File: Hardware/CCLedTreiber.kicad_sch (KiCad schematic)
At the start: 7 parts, among them U4 SY7200AABC

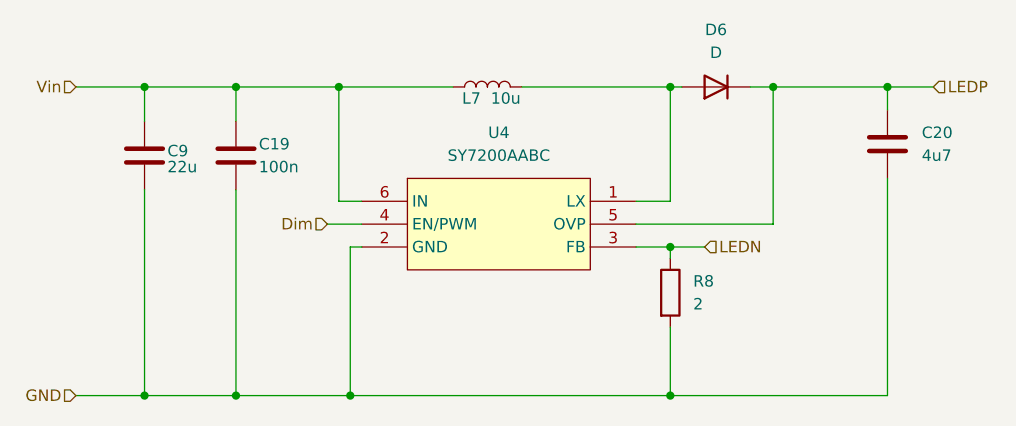
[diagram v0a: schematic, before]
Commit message: assign most LCSC numbers
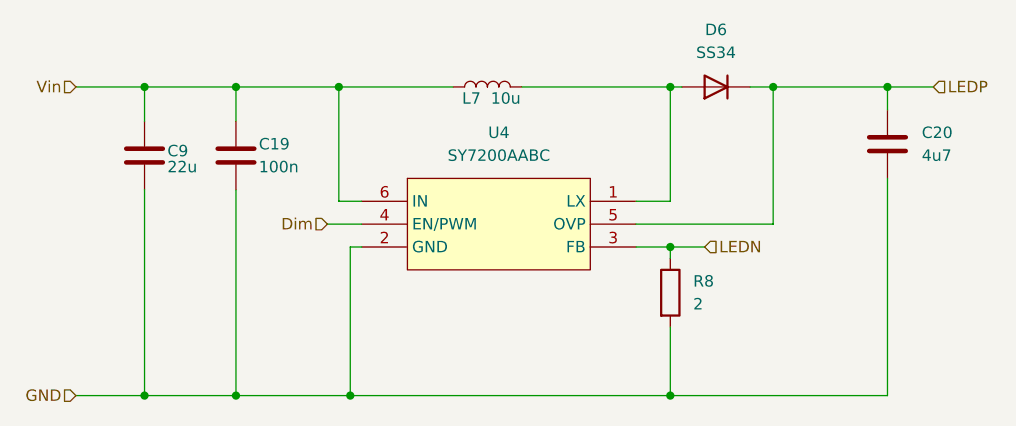
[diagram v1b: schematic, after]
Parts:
- C20: footprint Capacitor_SMD:C_1210_3225Metric -> Capacitor_SMD:C_1206_3216Metric
- D6: value D -> SS34
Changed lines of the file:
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@@
 			)
 		)
-		(property "Footprint" "Capacitor_SMD:C_1210_3225Metric"
+		(property "Footprint" "Capacitor_SMD:C_1206_3216Metric"
 			(at 150.8252 66.04 0)
 			(effects
@@
 			)
 		)
-		(property "Value" "D"
+		(property "Value" "SS34"
 			(at 130.81 52.07 0)
 			(effects

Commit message: assign remaining LCSC numbers and change R_sense of LED drivers
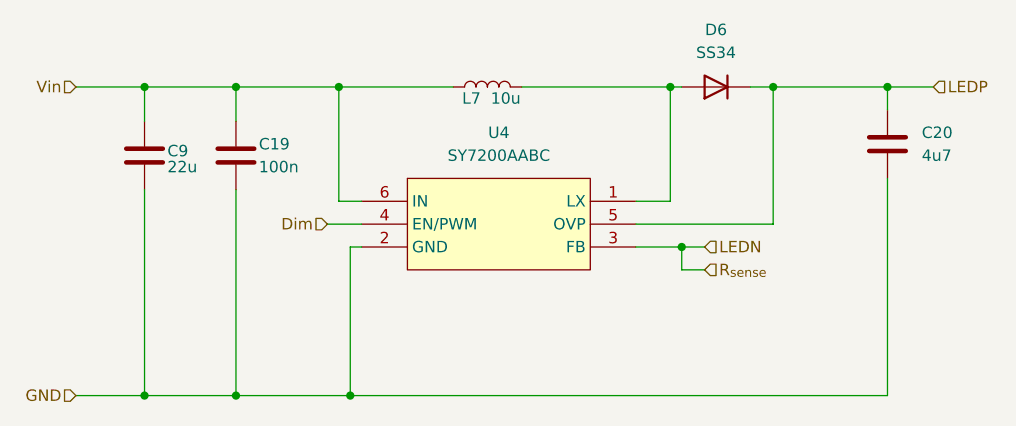
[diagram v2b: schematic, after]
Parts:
- removed R8: 2, Resistor_SMD:R_0805_2012Metric, symbol Device:R
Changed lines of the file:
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@@
 	)
 	(junction
-		(at 125.73 90.17)
-		(diameter 0)
-		(color 0 0 0 0)
-	)
-	(junction
-		(at 125.73 73.66)
+		(at 127 73.66)
 		(diameter 0)
 		(color 0 0 0 0)
@@
 	(wire
 		(pts
-			(xy 90.17 90.17) (xy 125.73 90.17)
-		)
-		(stroke
-			(width 0)
-			(type default)
-		)
-	)
-	(wire
-		(pts
-			(xy 125.73 90.17) (xy 149.86 90.17)
+			(xy 90.17 90.17) (xy 149.86 90.17)
+		)
+		(stroke
+			(width 0)
+			(type default)
+		)
+	)
+	(wire
+		(pts
+			(xy 127 73.66) (xy 129.54 73.66)
+		)
+		(stroke
+			(width 0)
+			(type default)
+		)
+	)
+	(wire
+		(pts
+			(xy 127 76.2) (xy 127 73.66)
 		)
 		(stroke
@@
 	(wire
 		(pts
-			(xy 125.73 73.66) (xy 125.73 74.93)
-		)
-		(stroke
-			(width 0)
-			(type default)
-		)
-	)
-	(wire
-		(pts
 			(xy 59.69 55.88) (xy 67.31 55.88)
 		)
@@
 	(wire
 		(pts
-			(xy 125.73 73.66) (xy 121.92 73.66)
-		)
-		(stroke
-			(width 0)
-			(type default)
-		)
-	)
-	(wire
-		(pts
 			(xy 91.44 68.58) (xy 88.9 68.58)
 		)
@@
 	(wire
 		(pts
-			(xy 125.73 82.55) (xy 125.73 90.17)
+			(xy 129.54 76.2) (xy 127 76.2)
 		)
 		(stroke
@@
 	(wire
 		(pts
-			(xy 129.54 73.66) (xy 125.73 73.66)
+			(xy 121.92 73.66) (xy 127 73.66)
 		)
 		(stroke
@@
 			(width 0)
 			(type default)
+		)
+	)
+	(hierarchical_label "R_{sense}"
+		(shape input)
+		(at 129.54 76.2 0)
+		(fields_autoplaced yes)
+		(effects
+			(font
+				(size 1.27 1.27)
+			)
+			(justify left)
 		)
 	)
@@
 					(unit 1)
 				)
-			)
-		)
-	)
-	(symbol
-		(lib_id "Device:R")
-		(at 125.73 78.74 0)
-		(unit 1)
-		(exclude_from_sim no)
-		(in_bom yes)
-		(on_board yes)
-		(dnp no)
-		(fields_autoplaced yes)
-		(property "Reference" "R8"
-			(at 128.27 77.4699 0)
-			(effects
-				(font
-					(size 1.27 1.27)
-				)
-				(justify left)
-			)
-		)
-		(property "Value" "2"
-			(at 128.27 80.0099 0)
-			(effects
-				(font
-					(size 1.27 1.27)
-				)
-				(justify left)
-			)
-		)
-		(property "Footprint" "Resistor_SMD:R_0805_2012Metric"
-			(at 123.952 78.74 90)
-			(effects
-				(font
-					(size 1.27 1.27)
-				)
-				(hide yes)
-			)
-		)
-		(property "Datasheet" "~"
-			(at 125.73 78.74 0)
-			(effects
-				(font
-					(size 1.27 1.27)
-				)
-				(hide yes)
-			)
-		)
-		(property "Description" "Resistor"
-			(at 125.73 78.74 0)
-			(effects
-				(font
-					(size 1.27 1.27)
-				)
-				(hide yes)
-			)
-		)
-		(pin "2"
-		)
-		(pin "1"
-		)
-		(instances
-			(project "LEDTischLampe"
-				(path "/34c772aa-2c68-48ca-93c3-7ad335c6d96d/510bc110-0bc9-4ffc-b901-498b8c9eef65/3158ee75-269d-4678-a09e-d51dcc288918"
-					(reference "R8")
-					(unit 1)
-				)
-				(path "/34c772aa-2c68-48ca-93c3-7ad335c6d96d/510bc110-0bc9-4ffc-b901-498b8c9eef65/9a951bb8-f46c-4ee0-a3d3-d4e6ca3ed117"
-					(reference "R26")
-					(unit 1)
-				)
-				(path "/34c772aa-2c68-48ca-93c3-7ad335c6d96d/510bc110-0bc9-4ffc-b901-498b8c9eef65/caa9cf2f-0db8-4b11-940e-edce255a092c"
-					(reference "R16")
-					(unit 1)
-				)
-				(path "/34c772aa-2c68-48ca-93c3-7ad335c6d96d/510bc110-0bc9-4ffc-b901-498b8c9eef65/fb3a6902-adb0-42f5-a319-4ea74339d4c7"
-					(reference "R27")
-					(unit 1)
-				)
-				(path "/34c772aa-2c68-48ca-93c3-7ad335c6d96d/5ca28fd6-5d3d-44e4-a7e8-e548f0114941/2a7edb5c-7ef0-4d35-9613-2c0a7f441272"
-					(reference "R9")
-					(unit 1)
-				)

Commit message: remove LCSC numbers from silkscreen (bug in jlcpcb-tools)
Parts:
- C19: LCSC (none) -> C307331
- C20: LCSC (none) -> C29823
- C9: LCSC (none) -> C52306
- D6: LCSC (none) -> C8678
- L7: LCSC (none) -> C5832376
- U4: LCSC (none) -> C107309
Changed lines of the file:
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@@
+			)
+		)
+		(property "LCSC" "C52306"
+			(at 69.85 62.992 0)
+			(effects
+				(font
+					(size 1.27 1.27)
+				)
+				(hide yes)
 			)
 		)
@@
 			)
 		)
+		(property "LCSC" "C107309"
+			(at 106.68 60.96 0)
+			(effects
+				(font
+					(size 1.27 1.27)
+				)
+				(hide yes)
+			)
+		)
 		(pin "2"
 		)
@@
 		(property "Description" ""
 			(at 105.41 55.88 0)
+			(effects
+				(font
+					(size 1.27 1.27)
+				)
+				(hide yes)
+			)
+		)
+		(property "LCSC" "C5832376"
+			(at 103.632 57.15 0)
 			(effects
 				(font
@@
 			)
 		)
+		(property "LCSC" "C29823"
+			(at 153.67 60.9599 0)
+			(effects
+				(font
+					(size 1.27 1.27)
+				)
+				(hide yes)
+			)
+		)
 		(pin "2"
 		)
@@
 			)
 		)
+		(property "LCSC" "C8678"
+			(at 130.81 49.53 0)
+			(effects
+				(font
+					(size 1.27 1.27)
+				)
+				(hide yes)
+			)
+		)
 		(pin "1"
 		)
@@
 			(effects
 				(font
+					(size 1.27 1.27)
+				)
+				(hide yes)
+			)
+		)
+		(property "LCSC" "C307331"
+			(at 80.01 62.23 0)
+			(effects
+				(font

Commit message: final touches for v1.0
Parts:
- C19: LCSC C307331 -> (none)
- C20: LCSC C29823 -> (none)
- C9: footprint Capacitor_SMD:C_1210_3225Metric -> Capacitor_SMD:C_0805_2012Metric; LCSC C52306 -> (none)
- D6: LCSC C8678 -> (none)
- L7: LCSC C5832376 -> (none)
- U4: LCSC C107309 -> (none)
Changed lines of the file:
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@@
 			)
 		)
-		(property "Footprint" "Capacitor_SMD:C_1210_3225Metric"
+		(property "Footprint" "Capacitor_SMD:C_0805_2012Metric"
 			(at 68.2752 67.31 0)
 			(effects
@@
 		(property "Description" "Unpolarized capacitor"
 			(at 67.31 63.5 0)
-			(effects
-				(font
-					(size 1.27 1.27)
-				)
-				(hide yes)
-			)
-		)
-		(property "LCSC" "C52306"
-			(at 69.85 62.992 0)
 			(effects
 				(font
@@
 			)
 		)
-		(property "LCSC" "C107309"
-			(at 106.68 60.96 0)
-			(effects
-				(font
-					(size 1.27 1.27)
-				)
-				(hide yes)
-			)
-		)
 		(pin "2"
 		)
@@
 		(property "Description" ""
 			(at 105.41 55.88 0)
-			(effects
-				(font
-					(size 1.27 1.27)
-				)
-				(hide yes)
-			)
-		)
-		(property "LCSC" "C5832376"
-			(at 103.632 57.15 0)
 			(effects
 				(font
@@
 			)
 		)
-		(property "LCSC" "C29823"
-			(at 153.67 60.9599 0)
-			(effects
-				(font
-					(size 1.27 1.27)
-				)
-				(hide yes)
-			)
-		)
 		(pin "2"
 		)
@@
 			)
 		)
-		(property "LCSC" "C8678"
-			(at 130.81 49.53 0)
-			(effects
-				(font
-					(size 1.27 1.27)
-				)
-				(hide yes)
-			)
-		)
 		(pin "1"
 		)
@@
 			(effects
 				(font
-					(size 1.27 1.27)
-				)
-				(hide yes)
-			)
-		)
-		(property "LCSC" "C307331"
-			(at 80.01 62.23 0)
-			(effects
-				(font

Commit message: some more tweaks (rotated input terminal block, added voltage measurement)
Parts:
- U4: LCSC Part C107309 -> (none)
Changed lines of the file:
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@@
-			)
-		)
-		(property "LCSC Part" "C107309"
-			(at 106.68 86.36 0)
-			(effects
-				(font
-					(size 1.27 1.27)
-				)
-				(hide yes)
 			)
 		)
